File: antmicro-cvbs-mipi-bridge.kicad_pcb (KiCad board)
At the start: 4 copper layers, 55 x 59.7 mm, 101 parts, among them IC1 ADV7280BCPZ-M, IC2 TLV70018, IC4 SN74AUP1G17DCKR, IC5 SN74AUP1G17DCKR, J1 WE_68715014522, J2 61300211121, J7 61300211121, Q1 NX3008NBKS_2, Q2 BSS138APW, Y1 ABM8G-28.63636MHZ-18-D2Y-T

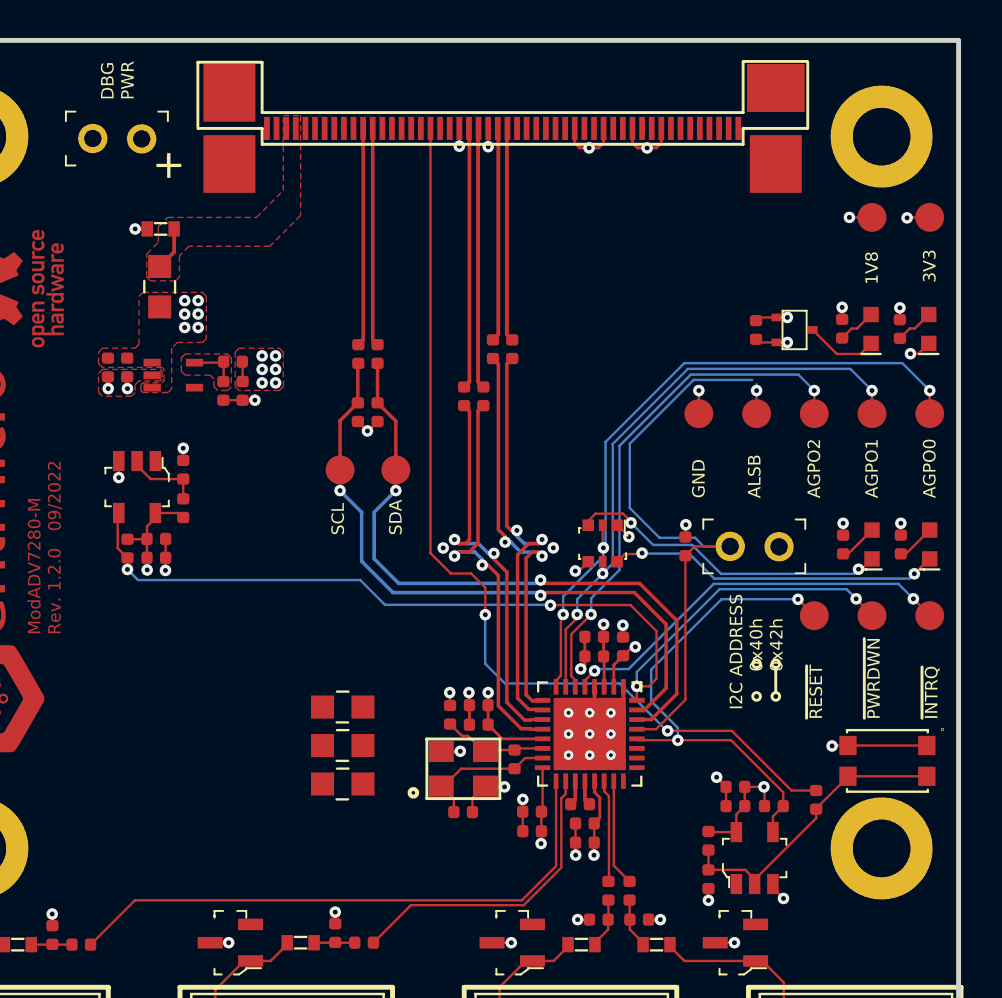
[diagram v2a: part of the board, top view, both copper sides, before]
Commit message: Finished and optimized routing on PCB
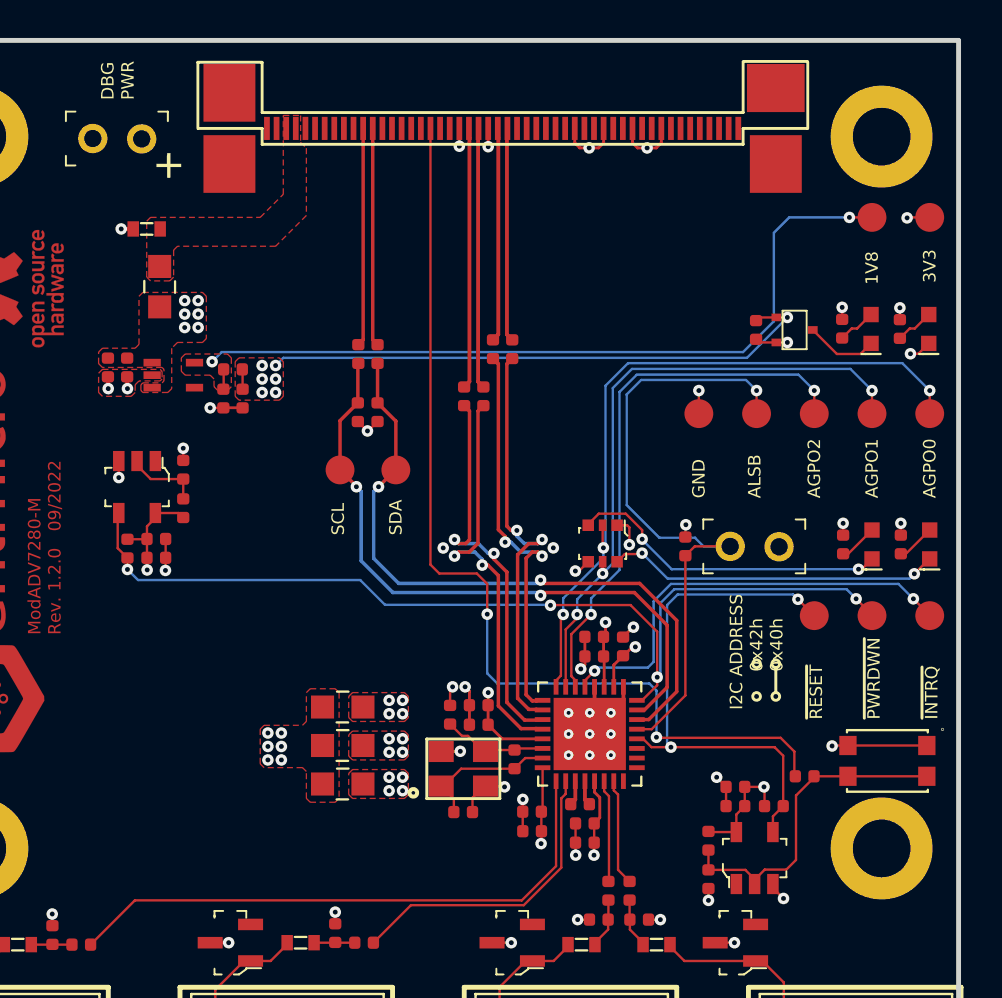
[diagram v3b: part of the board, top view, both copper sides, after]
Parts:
- moved R29 1.36 mm to (158.7, 94.2), turned to 0 degrees
- moved C12 0.72 mm to (124.5, 65.8)
- moved C26 0.40 mm to (129.5, 74.6)
- moved C9 0.40 mm to (128.5, 74.6)
- moved R30 0.40 mm to (129.0, 73.1)
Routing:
- net Net-(C9-Pad1): track 3.75 -> 41.4 mm, vias 1 -> 2
- net 1V8_SYS: track 2.73 -> 30.4 mm, vias 7 -> 13
- net GND: track 53.1 -> 55.7 mm
- net /RESET: track 25.6 -> 28.0 mm
- net Net-(C12-Pad1): track 2.26 -> 0.00 mm
- net Net-(IC1-Pad5): track 21.0 -> 22.9 mm
- net /ALSB: track 31.8 -> 33.6 mm
- net /AGPO0: track 35.3 -> 37.0 mm
- net /AGPO1: track 31.0 -> 32.7 mm
- net Net-(C21-Pad1): track 15.6 -> 17.3 mm
- net Net-(IC1-Pad6): track 26.8 -> 28.5 mm
- net /RST_IN: track 49.6 -> 51.1 mm
- net DVDD_1V8: track 8.08 -> 8.22 mm, vias 2 -> 6
- net PVDD_1V8: vias 1 -> 5
- net AVDD_1V8: vias 1 -> 5
- added copper zone on In2.Cu, net 1V8_SYS
- added copper zone on F.Cu, net AVDD_1V8
- added copper zone on In2.Cu, net AVDD_1V8
- added copper zone on F.Cu, net DVDD_1V8
- added copper zone on In2.Cu, net DVDD_1V8
- added copper zone on F.Cu, net PVDD_1V8
- added copper zone on In2.Cu, net PVDD_1V8
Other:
- board text added: "I2C ADDRESS 0x42h 0x40h"
- board text removed: "I2C ADDRESS 0x40h 0x42h"

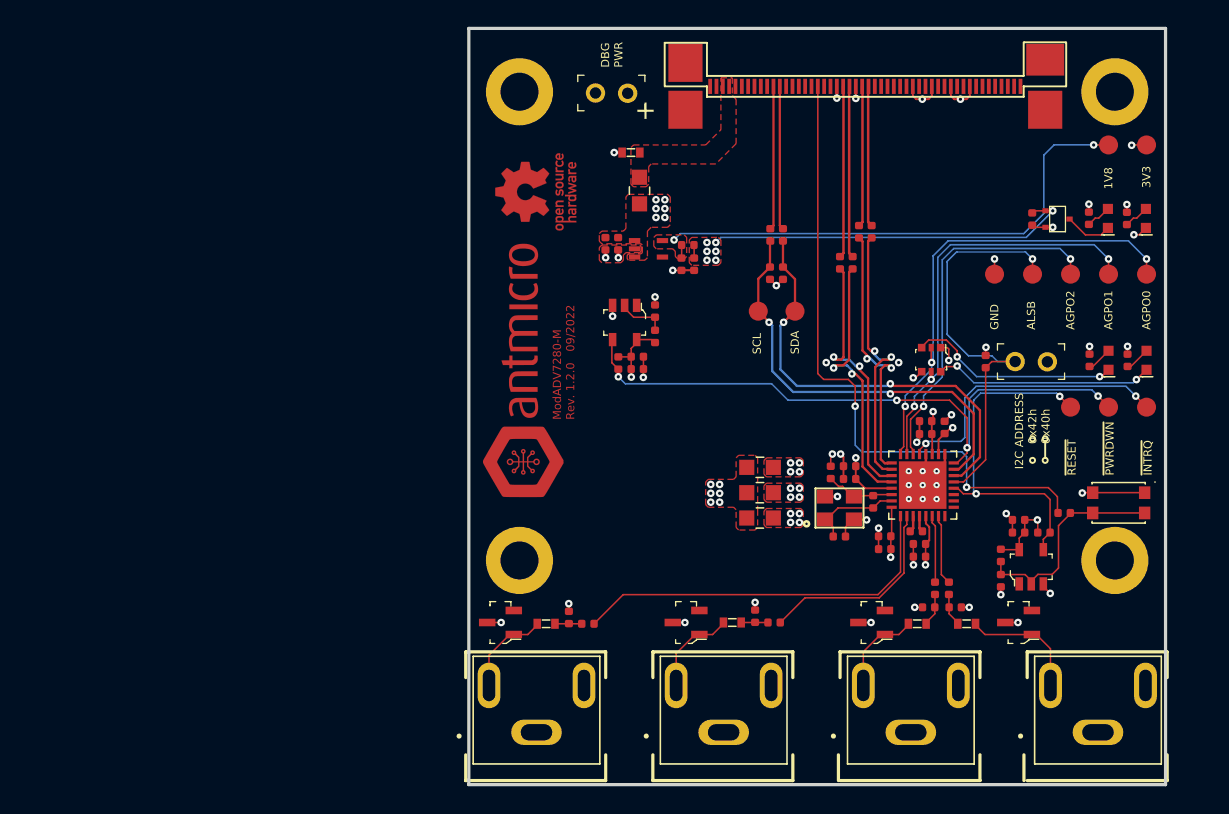
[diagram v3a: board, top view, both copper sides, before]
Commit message: Corrected PCB after review
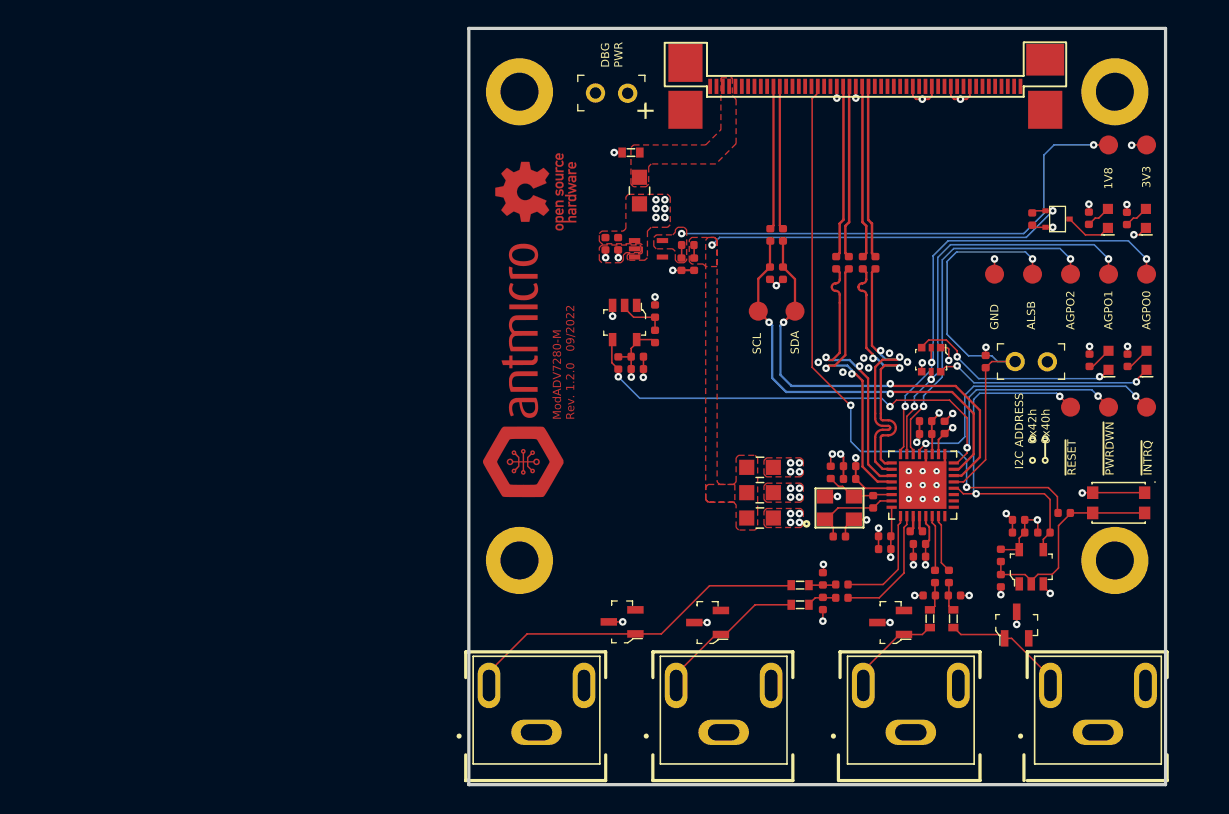
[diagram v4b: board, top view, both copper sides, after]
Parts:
- moved C1 20.3 mm to (141.2, 99.9)
- moved R3 20.3 mm to (139.7, 99.5)
- moved R1 20.3 mm to (137.8, 100.0)
- moved D1 9.60 mm to (123.8, 102.8)
- moved C2 5.69 mm to (141.2, 101.0)
- moved R4 5.53 mm to (137.8, 101.5)
- moved R5 5.44 mm to (139.7, 101.4), turned to 90 degrees
- moved R22 2.47 mm to (143.8, 74.5)
- moved R23 2.47 mm to (142.8, 74.5)
- moved D2 1.70 mm to (130.6, 102.9)
- moved D3 1.50 mm to (145.0, 102.9)
- moved R10 1.12 mm to (149.9, 102.6), turned to 90 degrees
- moved R8 1.08 mm to (148.1, 102.6), turned to 90 degrees
- moved R11 0.94 mm to (150.0, 100.8)
- moved R9 0.94 mm to (148.1, 100.8)
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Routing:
- net /AIN1: track 30.3 -> 8.68 mm
- net /AIN1_ESD: track 7.28 -> 28.1 mm
- net /AIN2: track 16.0 -> 9.81 mm
- net /AIN2_ESD: track 7.32 -> 12.2 mm
- net /CSI_A_D0_R_N: track 11.1 -> 13.7 mm
- net /CSI_A_D0_R_P: track 11.1 -> 13.7 mm
- net /CSI_A_CLK_P: track 20.7 -> 22.0 mm
- net /AIN3: track 5.33 -> 4.39 mm
- net /AIN4: track 5.55 -> 4.62 mm
- net /RST_IN: track 51.1 -> 50.3 mm
- net /CSI_A_D0_P: track 21.2 -> 22.0 mm
- net Net-(C9-Pad1): track 41.4 -> 40.6 mm
- net /CSI_A_CLK_N: track 21.4 -> 22.1 mm
- net /AIN3_ESD: track 7.19 -> 7.83 mm
- net 1V8_SYS: track 30.4 -> 30.7 mm, vias 13 -> 2
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- added copper zone on In2.Cu, net GND
- removed copper zone on In2.Cu, net 1V8_SYS

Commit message: loclib. Added new components from schematic after review
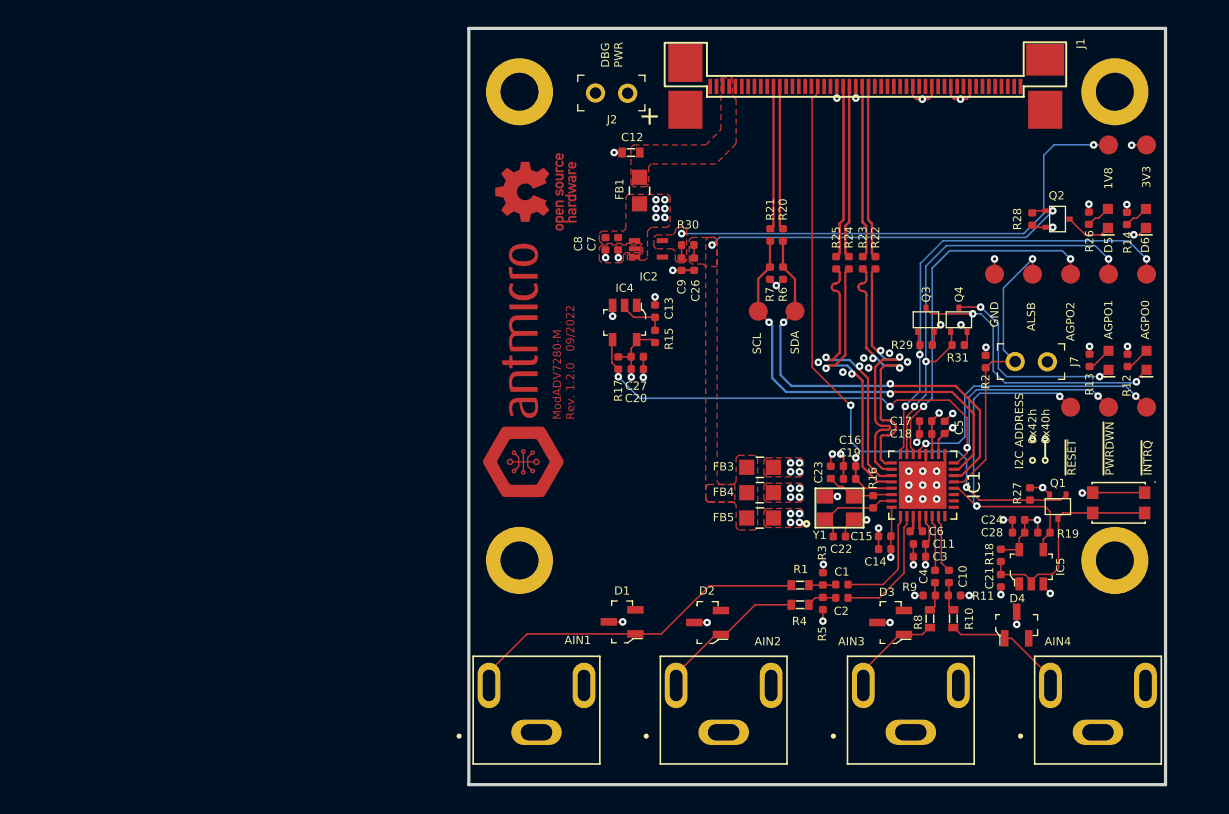
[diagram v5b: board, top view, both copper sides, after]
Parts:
- added Q3: BSS138APW, antmicro-cvbs-mipi-bridge-footprints:SC70-3, F.Cu at (147.8, 79.0)
- added Q4: BSS138APW, antmicro-cvbs-mipi-bridge-footprints:SC70-3, F.Cu at (150.4, 79.0)
- added R27: R_100k_0402, antmicro-cvbs-mipi-bridge-footprints:0402-res, F.Cu at (156.0, 92.8)
- added R31: R_100k_0402, antmicro-cvbs-mipi-bridge-footprints:0402-res, F.Cu at (150.3, 81.0)
- AGPO0, AGPO1, D5, D6: footprint antmicro-footprints:LED_0603 -> antmicro-cvbs-mipi-bridge-footprints:LED_0603
- AIN1, AIN2, AIN3, AIN4: footprint antmicro-footprints:PJRAN1X1U01X -> antmicro-cvbs-mipi-bridge-footprints:PJRAN1X1U01X
- C1, C10, C11, C13, C14, C15, C16, C17, C18, C19, C2, C20, C21, C22, C23, C24, C26, C27, C28, C3, C4, C5, C6, C7, C8, C9: footprint antmicro-footprints:0402-cap -> antmicro-cvbs-mipi-bridge-footprints:0402-cap
- C12: footprint antmicro-footprints:0603-cap -> antmicro-cvbs-mipi-bridge-footprints:0603-cap
- D1, D2, D3, D4: footprint antmicro-footprints:SOT-23-3 -> antmicro-cvbs-mipi-bridge-footprints:SOT-23-3
- FB1, FB3, FB4, FB5: footprint antmicro-footprints:0805-res -> antmicro-cvbs-mipi-bridge-footprints:0805-res
- IC1: footprint antmicro-footprints:LFCSP-32-1EP-5x5mm -> antmicro-cvbs-mipi-bridge-footprints:LFCSP-32-1EP-5x5mm
- IC2: footprint antmicro-footprints:SC-70-5 -> antmicro-cvbs-mipi-bridge-footprints:SC-70-5
- IC4, IC5: footprint antmicro-footprints:SOT-753 -> antmicro-cvbs-mipi-bridge-footprints:SOT-753
- J1: footprint antmicro-footprints:WE_68715014522 -> antmicro-cvbs-mipi-bridge-footprints:WE_68715014522
- J2, J7: footprint antmicro-footprints:PinHeader_1x2_P2.54_Drill0.9mm -> antmicro-cvbs-mipi-bridge-footprints:PinHeader_1x2_P2.54_Drill0.9mm
- MP1, MP2, MP3, MP4: footprint antmicro-footprints:9774030243R -> antmicro-cvbs-mipi-bridge-footprints:9774030243R
- N1: footprint antmicro-footprints:antmicro-logo_scaled_20mm -> antmicro-cvbs-mipi-bridge-footprints:antmicro-logo_scaled_20mm
- N2: footprint antmicro-footprints:oshw-logo -> antmicro-cvbs-mipi-bridge-footprints:oshw-logo
- Q1: value NX3008NBKS_2 -> BSS138APW; footprint antmicro-footprints:SOT-363 -> antmicro-cvbs-mipi-bridge-footprints:SC70-3
- Q2: footprint antmicro-footprints:SC70-3 -> antmicro-cvbs-mipi-bridge-footprints:SC70-3
- R1, R10, R4, R8: footprint antmicro-footprints:0603-res -> antmicro-cvbs-mipi-bridge-footprints:0603-res
- R11, R12, R13, R14, R15, R16, R17, R18, R19, R2, R20, R21, R22, R23, R24, R25, R26, R28, R3, R30, R5, R6, R7, R9: footprint antmicro-footprints:0402-res -> antmicro-cvbs-mipi-bridge-footprints:0402-res
- R29: value R_1k_0402 -> R_100k_0402; footprint antmicro-footprints:0402-res -> antmicro-cvbs-mipi-bridge-footprints:0402-res
- S1: footprint antmicro-footprints:SW_SPST_4.2x2.8 -> antmicro-cvbs-mipi-bridge-footprints:SW_SPST_4.2x2.8
- TP1, TP10, TP11, TP12, TP13, TP2, TP3, TP5, TP6, TP7, TP8, TP9: footprint antmicro-footprints:TP-R-1.5 -> antmicro-cvbs-mipi-bridge-footprints:TP-R-1.5
- Y1: footprint antmicro-footprints:KX-7 -> antmicro-cvbs-mipi-bridge-footprints:KX-7
- moved R29 17.2 mm to (147.8, 81.0), turned to 180 degrees
- moved Q1 15.3 mm to (158.2, 93.8), turned to -90 degrees
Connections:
- Q1 pad 1: GND -> /RST_IN
- Q1 pad 2: /AGPO0 -> GND
- Q1 pad 3: Net-(AGPO1-Pad2) -> Net-(C21-Pad1)
- R29 pad 1: /RST_IN -> GND
- R29 pad 2: Net-(C21-Pad1) -> /AGPO0
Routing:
- net /ALSB: track 33.6 -> 23.7 mm
- net Net-(AGPO0-Pad2): track 17.5 -> 22.5 mm
- net /AGPO1: track 32.7 -> 35.7 mm
- net /AIN2_ESD: track 12.2 -> 10.6 mm
- net /AIN3_ESD: track 7.83 -> 6.27 mm
- net /AIN1_ESD: track 28.1 -> 26.6 mm
- net GND: track 55.7 -> 54.6 mm, vias 51 -> 52
- net /RST_IN: track 50.3 -> 49.3 mm
- net /AIN4_ESD: track 9.94 -> 9.24 mm
- net Net-(AGPO1-Pad2): track 16.9 -> 16.3 mm
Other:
- board text removed: "AGPO0"
- board text removed: "AGPO1"

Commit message: Corrected ADV7280 footprint. Finished corrections and optimizations. Added missing step model
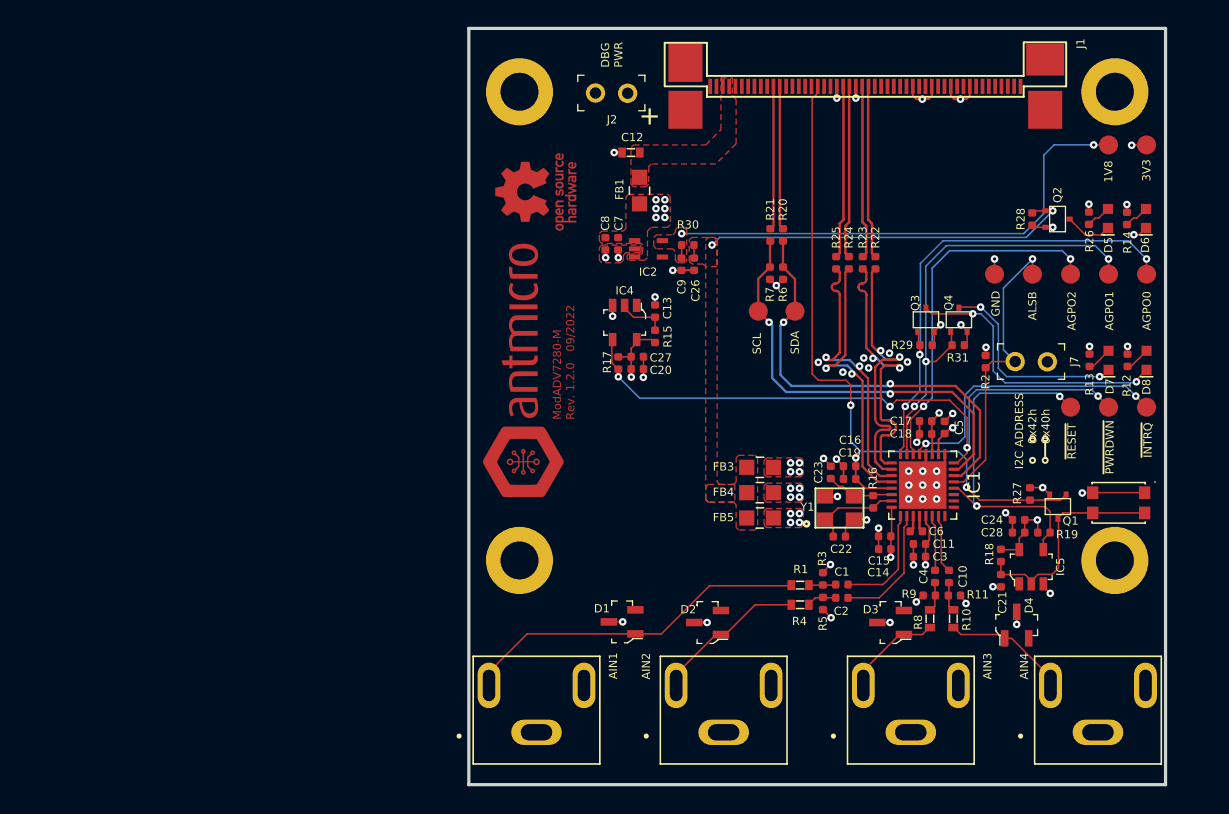
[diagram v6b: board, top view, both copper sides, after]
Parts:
- removed AGPO0, AGPO1: KP-1608ZGC, antmicro-cvbs-mipi-bridge-footprints:LED_0603
- added D7: KP-1608ZGC, antmicro-cvbs-mipi-bridge-footprints:LED_0603, F.Cu at (162.2, 82.2)
- added D8: KP-1608ZGC, antmicro-cvbs-mipi-bridge-footprints:LED_0603, F.Cu at (165.2, 82.2)
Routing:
- net /RST_IN: track 49.3 -> 50.6 mm
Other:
- board text added: "AGPO0"
- board text added: "AGPO1"
